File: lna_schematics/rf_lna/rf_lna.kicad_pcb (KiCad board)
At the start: 4 copper layers, 56 parts, among them J1 Conn_01x02_Pin, J2 Conn_Coaxial_Small, J3 Conn_Coaxial_Small, J4 Conn_01x02_Pin, J5 Conn_Coaxial_Small, J6 Conn_Coaxial_Small, U1 L78L05_SOT89, U3 BFP640, U5 L78L05_SOT89, U6 BFP640, U7 BFP640, U8 BFP640

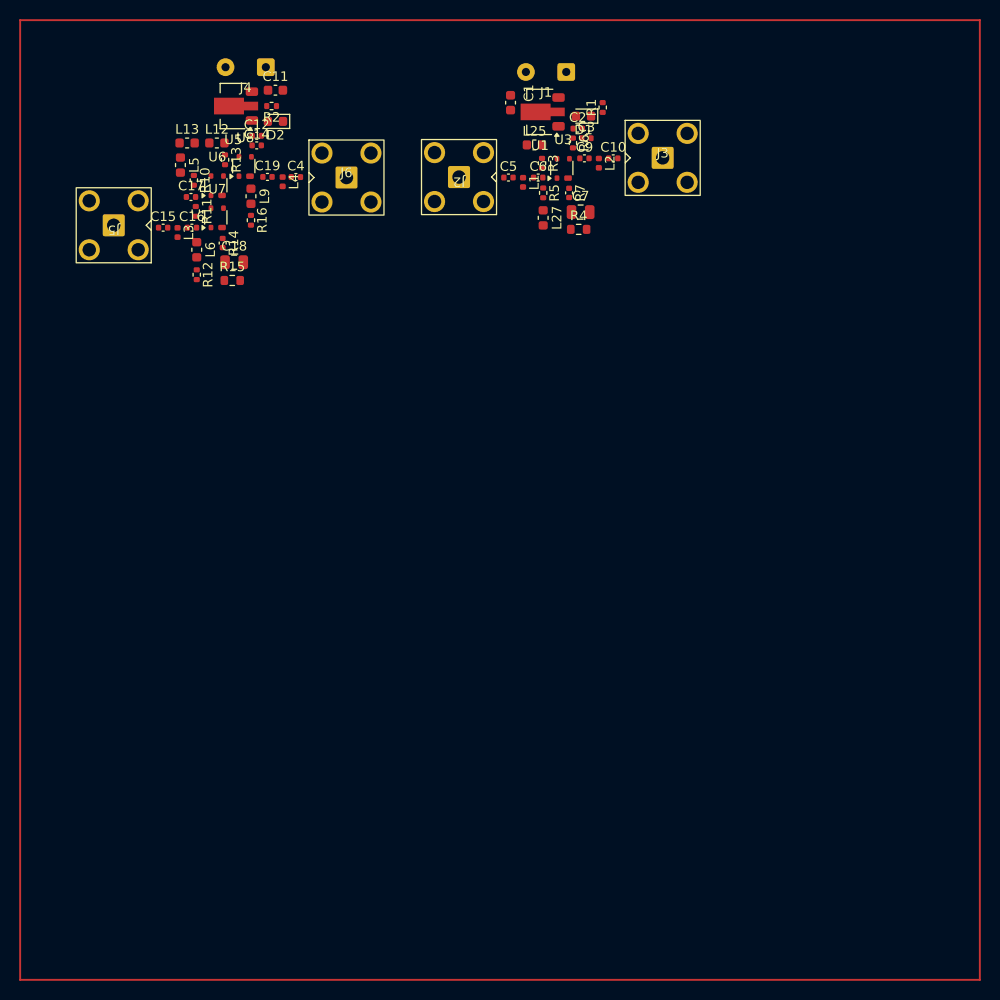
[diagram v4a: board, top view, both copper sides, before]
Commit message: [kicad] Added antenna footprint to PCB | TODO: simulate and then add the antenna to the gerber as a whole
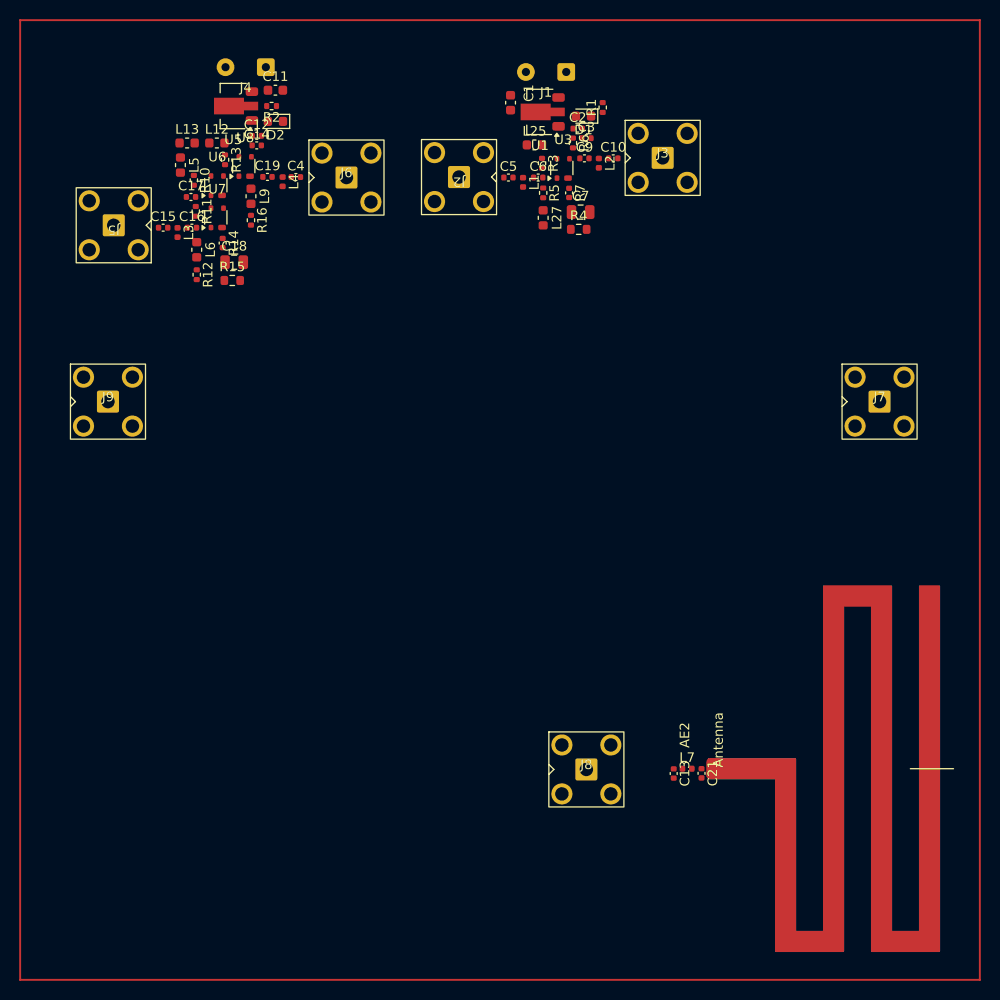
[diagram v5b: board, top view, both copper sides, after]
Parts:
- added AE2: Antenna, antennas:dn024, F.Cu at (121.8, 128.0)
- added C13: ~, Capacitor_SMD:C_0402_1005Metric, F.Cu at (118.1, 128.5)
- added C21: 2.7pF, Capacitor_SMD:C_0402_1005Metric, F.Cu at (121.0, 128.5)
- added J7: Conn_Coaxial_Small, Library:SMA_Amphenol_901-143_Vertical, F.Cu at (139.6, 89.8)
- added J8: Conn_Coaxial_Small, Library:SMA_Amphenol_901-143_Vertical, F.Cu at (109.0, 128.1)
- added J9: Conn_Coaxial_Small, Library:SMA_Amphenol_901-143_Vertical, F.Cu at (59.1, 89.8)
- added L7: 1.8nH, Inductor_SMD:L_0402_1005Metric, F.Cu at (119.5, 128.0)
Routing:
- net GND: track 20.4 -> 10.2 mm
- net /cascode/casc_out: track 30.9 -> 25.8 mm
